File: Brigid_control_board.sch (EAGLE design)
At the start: 28 parts, among them J1 ARDUINO_R3_SHIELD, P1 39-30-02, P2 39-30-02, P3 39-30-02, P4 39-30-02, P5 39-30-02, P6 39-30-02, P7 39-30-02, Q1 T460, Q2 T460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

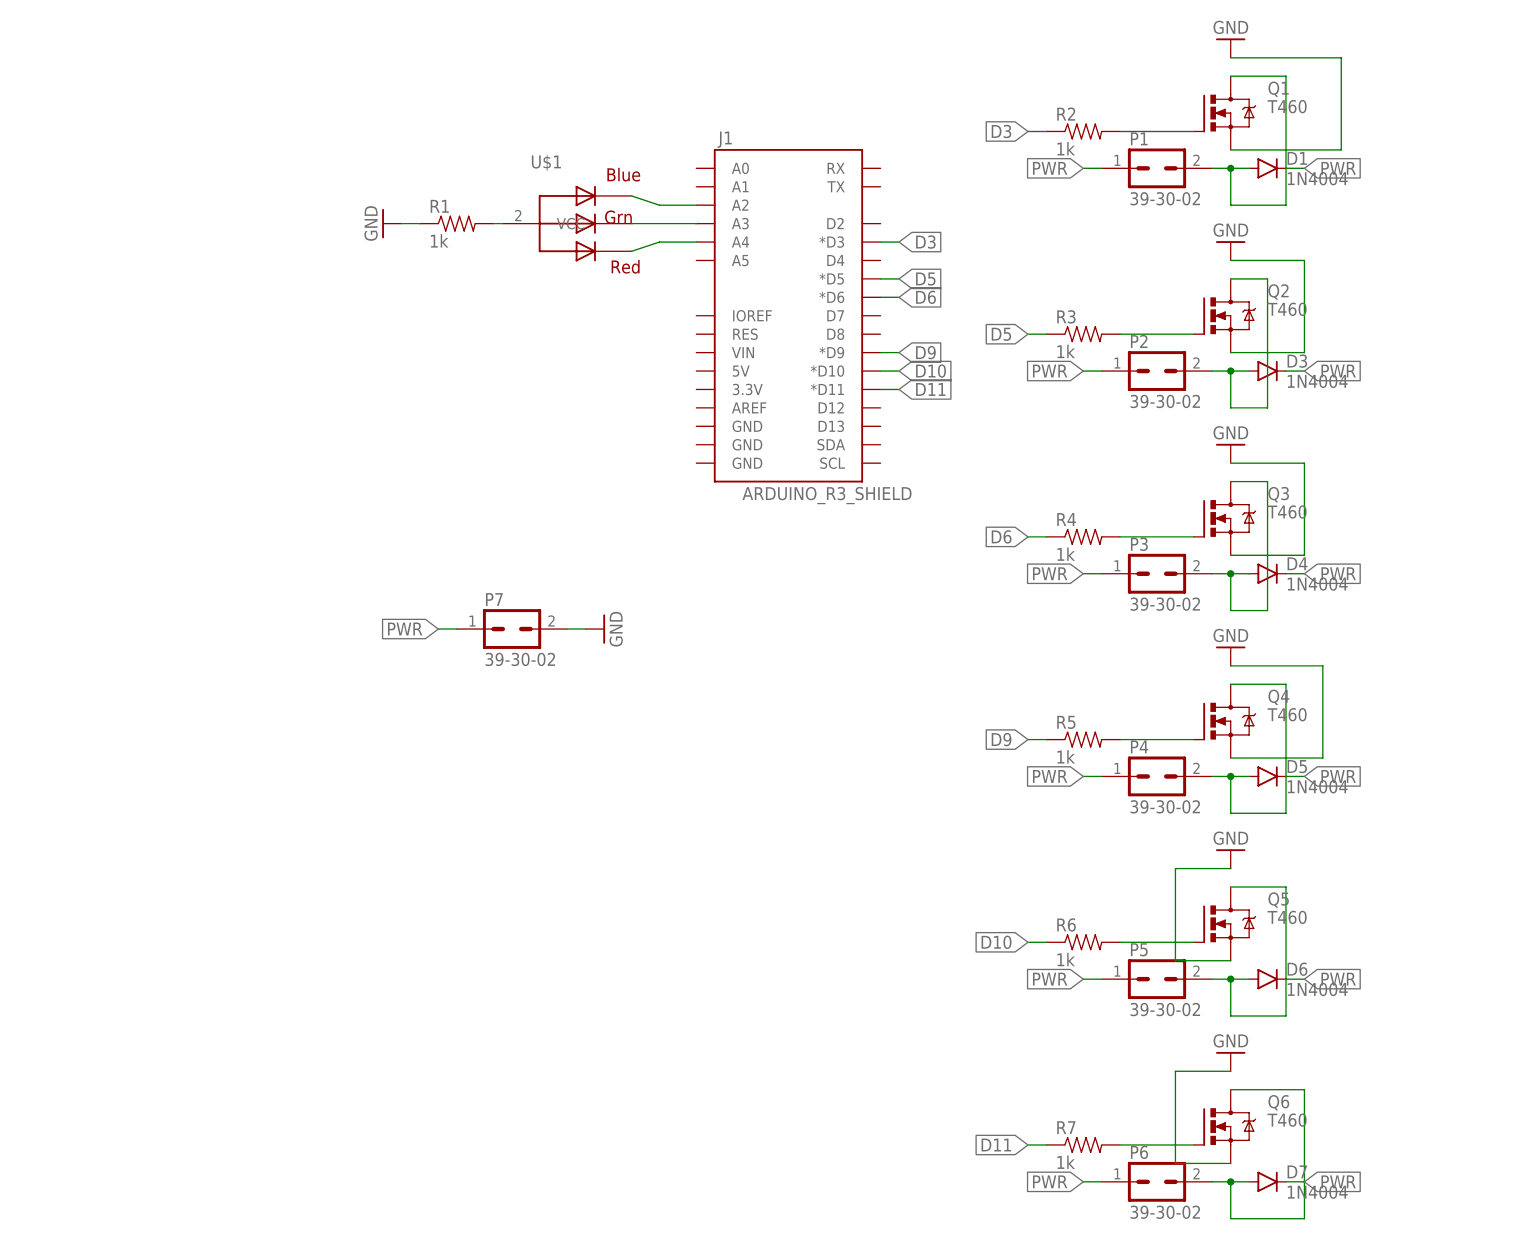
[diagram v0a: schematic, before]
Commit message: made brigid rev 2, created LED version of code
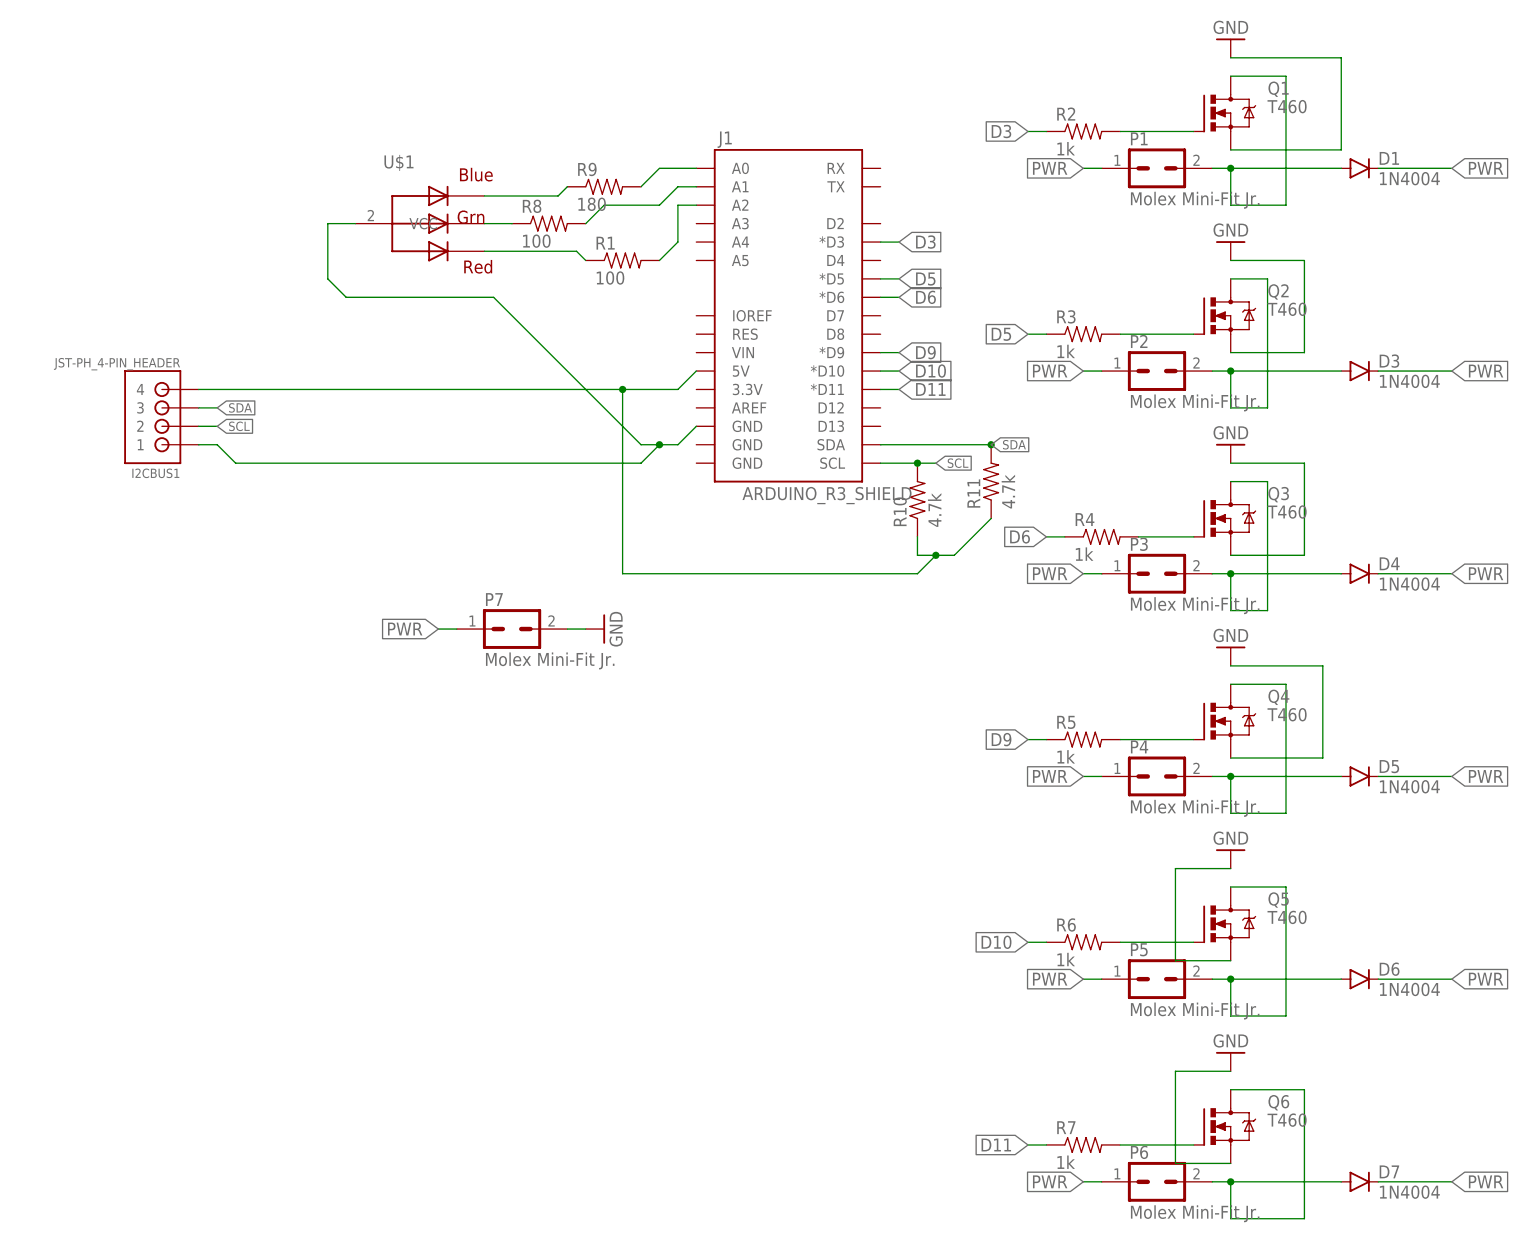
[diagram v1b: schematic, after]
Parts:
- added I2CBUS1: JST-PH_4-PIN_HEADER, JST_connectors:JST-PH_4-PIN_HEADER
- added R10, R11: 4.7k, SparkFun-Passives:RESISTOREZ
- added R8: 100, SparkFun-Passives:RESISTOREZ
- added R9: 180, SparkFun-Passives:RESISTOREZ
- P1, P2, P3, P4, P5, P6, P7: value 39-30-02 -> Molex Mini-Fit Jr.
- R1: value 1k -> 100
- U$1: value RGBLED_CA -> RGB LED
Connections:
- new net N$1: J1.A0, R9.2
- new net N$17: I2CBUS1.4, J1.5V, R10.1, R11.1
- new net N$20: I2CBUS1.1, J1.GND@2, U$1.VCC
- new net N$7: R1.1, U$1.RED
- new net SCL: I2CBUS1.2, J1.SCL, R10.2
- new net SDA: I2CBUS1.3, J1.SDA, R11.2
- net GND: no longer R1.1
- net N$2: now also J1.A1, R8.2; no longer J1.A2, U$1.BLUE
- net N$4: now also J1.A2, R1.2; no longer J1.A4, U$1.RED
- net N$5: now also R9.1, U$1.BLUE; no longer J1.A3, U$1.GREEN
- net N$8: now also R8.1, U$1.GREEN; no longer R1.2, U$1.VCC
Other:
- moved on the sheet: D1, D3, D4, D5, D6, D7, R1, R4, U$1
